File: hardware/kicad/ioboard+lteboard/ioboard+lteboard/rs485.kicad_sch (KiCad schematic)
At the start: 13 parts, among them J6 Conn_01x03, U15 TD321S485H-A, U16 ACM2520-301-2P

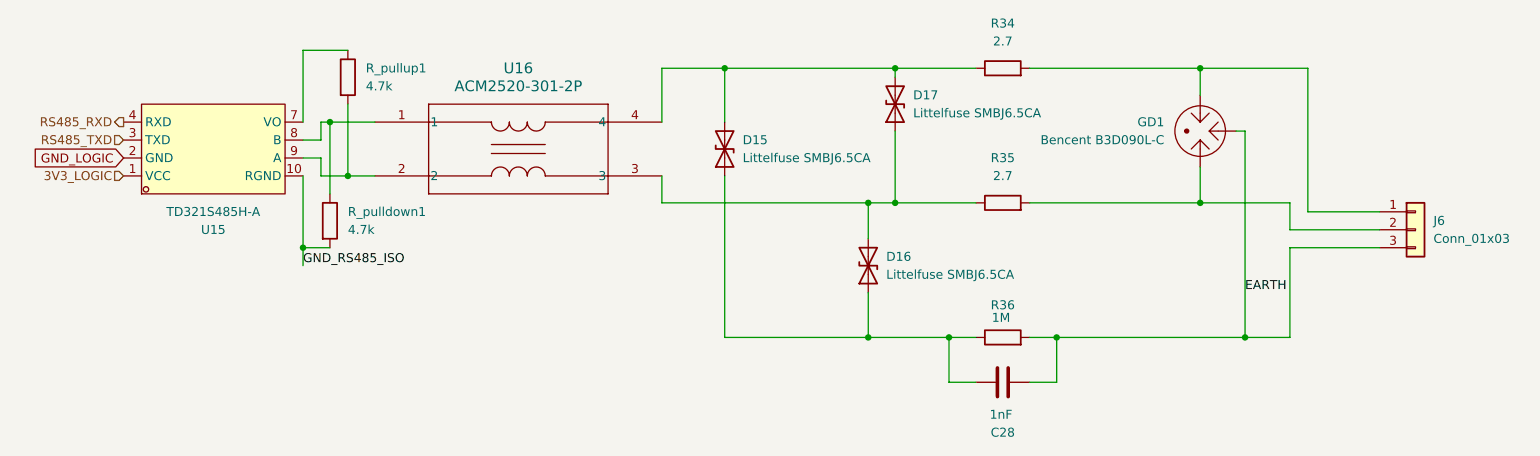
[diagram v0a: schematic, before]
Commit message: Close roadmap steps 6/7: pin assignment, board-to-board wiring, ERC pass clean; update docs to match
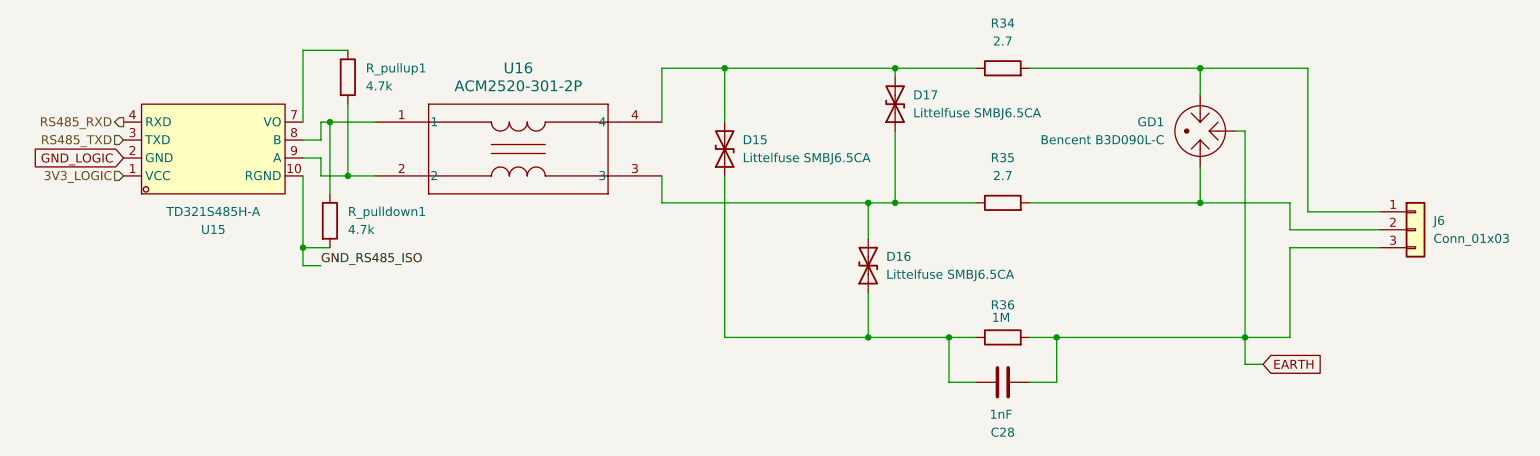
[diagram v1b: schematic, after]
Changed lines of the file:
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@@
+	(wire
+		(pts
+			(xy 66.04 68.58) (xy 68.58 68.58)
+		)
+		(stroke
+			(width 0)
+			(type default)
+		)
+	)
 	(wire
 		(pts
@@
 	(wire
 		(pts
+			(xy 199.39 78.74) (xy 199.39 82.55)
+		)
+		(stroke
+			(width 0)
+			(type default)
+		)
+	)
+	(wire
+		(pts
 			(xy 161.29 59.69) (xy 149.86 59.69)
 		)
@@
 	(wire
 		(pts
+			(xy 199.39 82.55) (xy 201.93 82.55)
+		)
+		(stroke
+			(width 0)
+			(type default)
+		)
+	)
+	(wire
+		(pts
 			(xy 205.74 63.5) (xy 205.74 59.69)
 		)
@@
 		)
 	)
-	(label "EARTH"
-		(at 199.39 72.39 0)
-		(effects
-			(font
-				(size 1.27 1.27)
-			)
-			(justify left bottom)
-		)
-	)
 	(label "GND_RS485_ISO"
-		(at 66.04 68.58 0)
+		(at 68.58 68.58 0)
 		(effects
 			(font
@@
 				(hide yes)
 			)
+		)
+	)
+	(global_label "EARTH"
+		(shape input)
+		(at 201.93 82.55 0)
+		(fields_autoplaced yes)
+		(effects
+			(font
+				(size 1.27 1.27)
+			)
+			(justify left)
+		)
+		(property "Intersheetrefs" "${INTERSHEET_REFS}"
+			(at 210.7209 82.55 0)
+			(effects
+				(font
+					(size 1.27 1.27)
+				)
+				(justify left)
+				(hide yes)
+			)
